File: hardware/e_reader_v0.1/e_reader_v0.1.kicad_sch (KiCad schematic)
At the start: 58 parts, among them J1 SD_Card, J2 Waveshare_7.5_EPD, Q3 DMG3415U, SW1 KMR2, SW2 KMR2, SW3 KMR2, SW4 KMR2, SW5 KMR2, SW6 KMR2, SW7 KMR2, SW8 KMR2, SW9 KMR2, U1 ESP32-S3-WROOM-1, U2 AP2112/RT9080-3.3, U3 MCP73831T-2ACI/OT, X1 JSTPH, X3 USB C

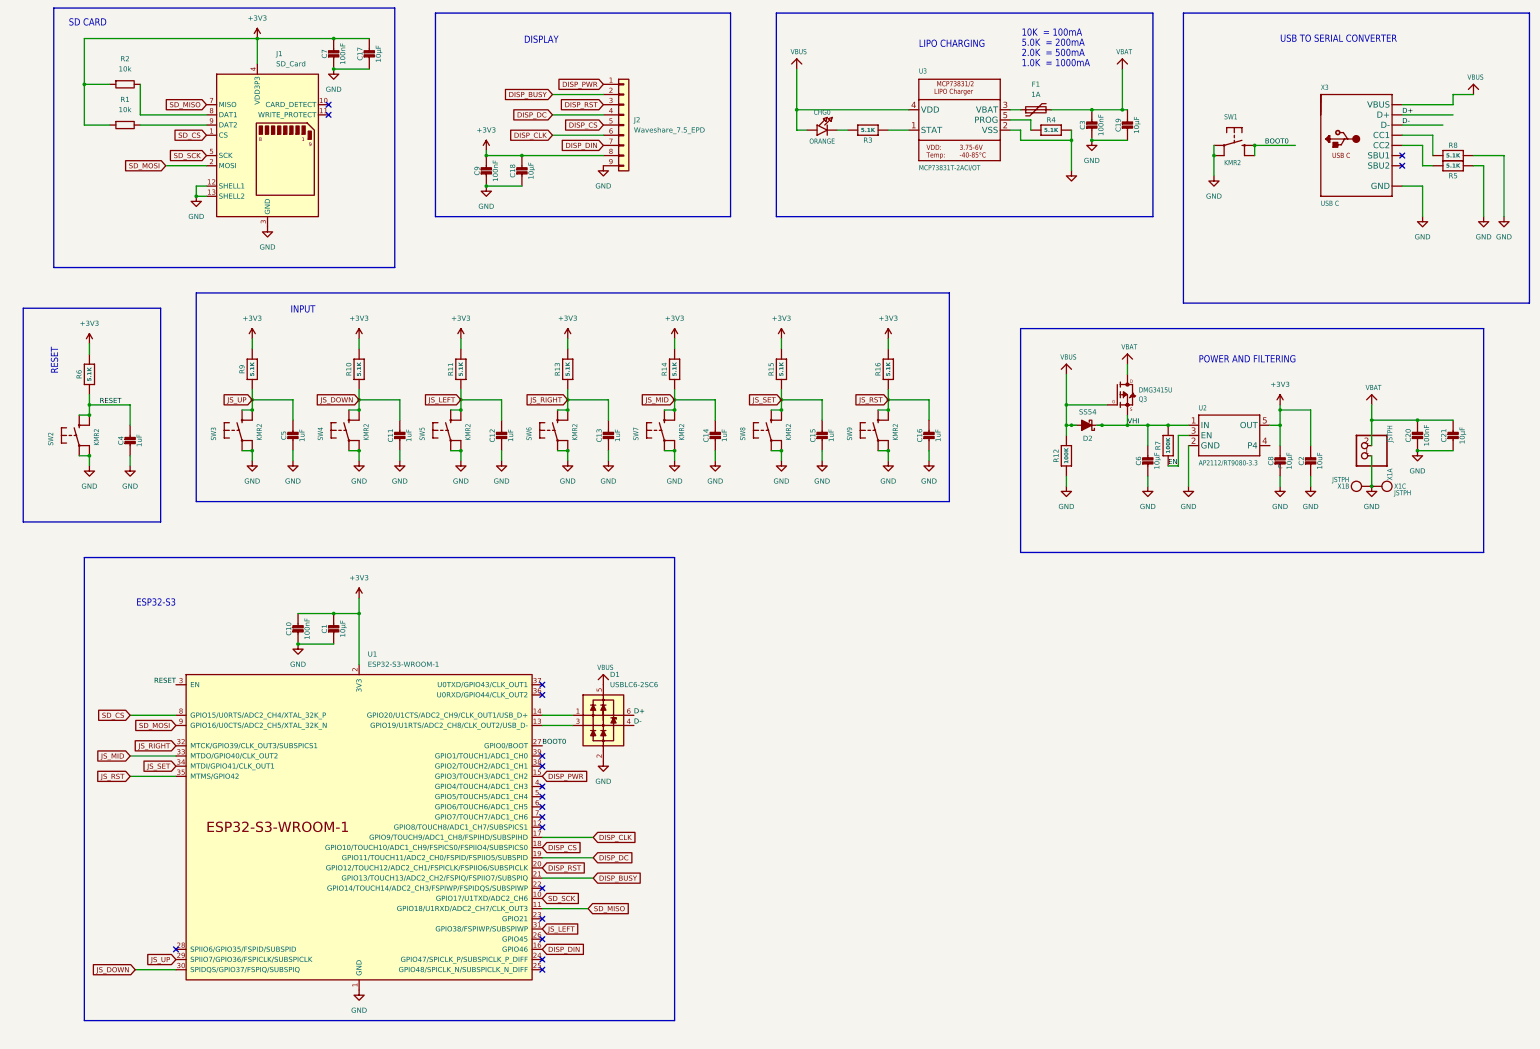
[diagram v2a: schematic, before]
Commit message: Fix footprints, add power switch and battery voltage divider
- Fix SW1-SW9 KMR2 footprints (were incorrectly set to USB-C)
- Add SW10 power switch (Nidec CAS-120A1)
- Add R17/R18 battery voltage divider (110K) for ADC battery monitoring
- Assign correct SOT-23-5 footprints to U2, U3
- Fix D2 SS54, D1 USBLC6, Q3 DMG3415U footprints

Co-Authored-By: Claude Sonnet 4.6 <noreply@anthropic.com>
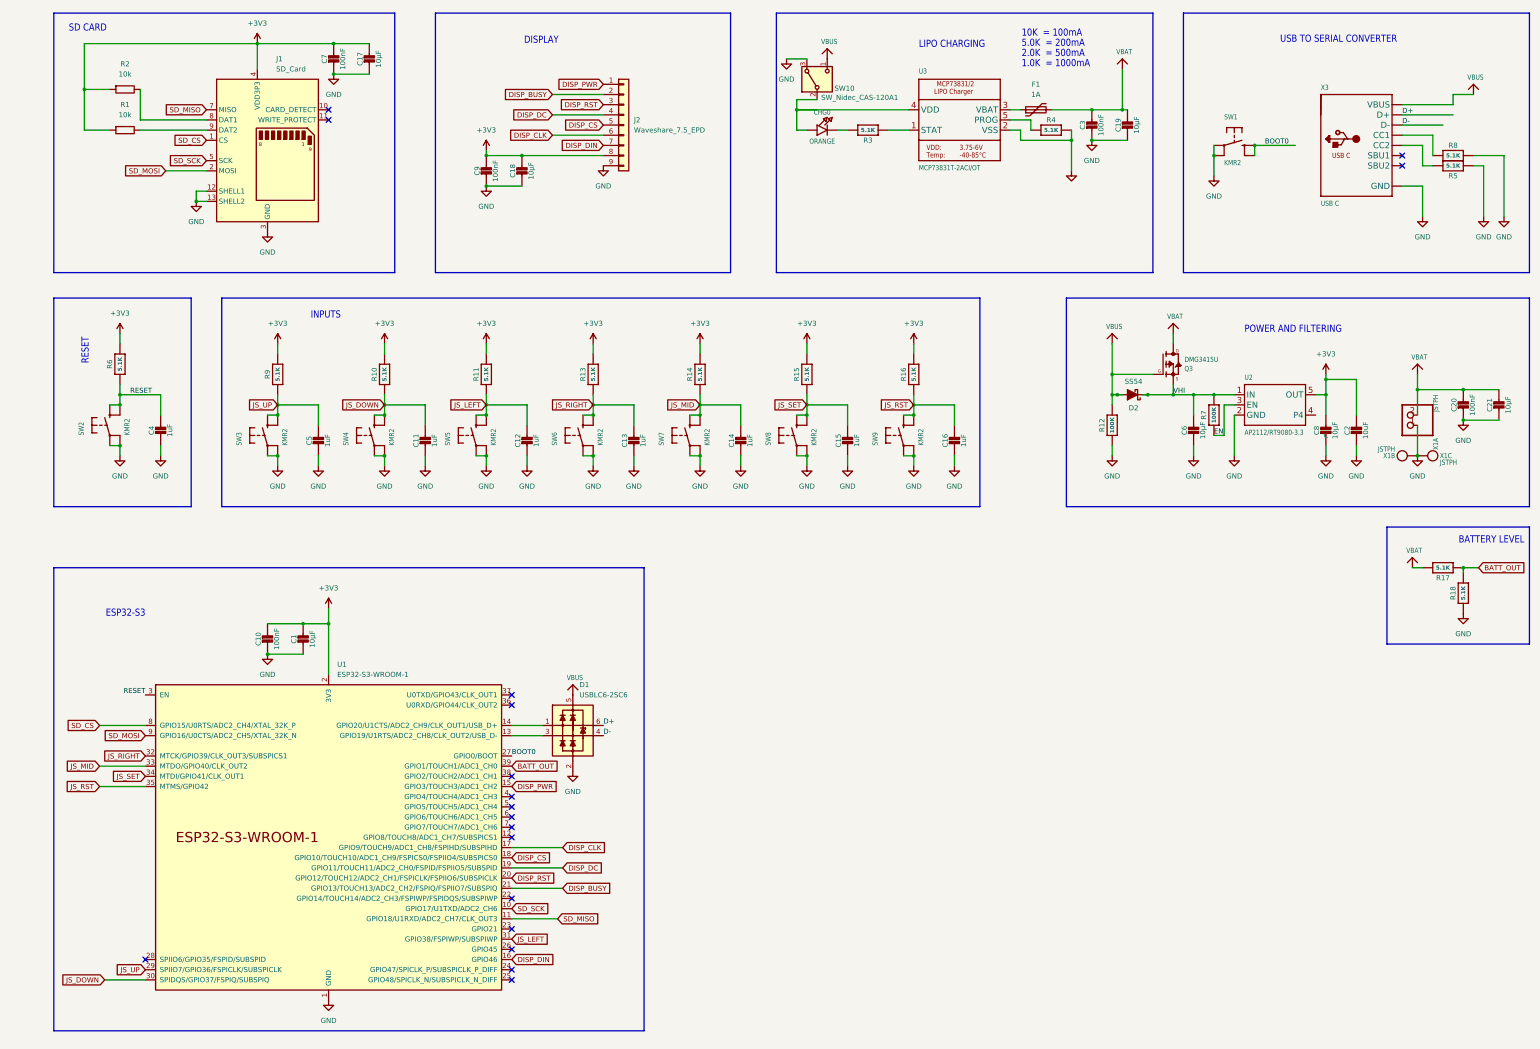
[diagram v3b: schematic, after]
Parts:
- added R17, R18: 5.1K, Resistor_SMD:R_0402_1005Metric, symbol Adafruit ESP32-S3 8MB No PSRAM-eagle-import:RESISTOR_0603_NOOUT
- added SW10: SW_Nidec_CAS-120A1, Button_Switch_SMD:Nidec_Copal_CAS-120A, symbol Switch:SW_Nidec_CAS-120A1
- C10: footprint Adafruit ESP32-S3 8MB No PSRAM:0603-NO -> Capacitor_SMD:C_0402_1005Metric
- C8: footprint Adafruit ESP32-S3 8MB No PSRAM:0805-NO -> Capacitor_SMD:C_0805_2012Metric
- CHG0: footprint Adafruit ESP32-S3 8MB No PSRAM:CHIPLED_0603_NOOUTLINE -> LED:LED_0603_1608Metric
- SW1, SW2, SW3, SW4, SW5, SW6, SW7, SW8, SW9: footprint Connector_USB:USB_C_Receptacle_HRO_TYPE-C-31-M-12 -> Button_Switch_SMD:SW_SPST_CK_KMR2
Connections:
- net GND: now also R18.1, SW10.3 (A)
- net VBAT: now also R17.2
- net VBUS: now also SW10.1 (C); no longer CHG0.A, U3.4 (VDD)
- net BATT_OUT: now reaches U1.39 (GPIO1/TOUCH1/ADC1_CH0)
- net BATT_OUT: now also R17.1, R18.2
- new net: CHG0.A, SW10.2 (B), U3.4 (VDD)
- no-connect marks 19 -> 18
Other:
- note added: "BATTERY LEVEL"
- note added: "INPUTS"
- note removed: "INPUT"
- moved on the sheet: C1, C10, C11, C12, C13, C14, C15, C16, C17, C2, C20, C21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
